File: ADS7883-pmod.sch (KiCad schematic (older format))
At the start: 16 parts, among them P1 CONN_01X03, P2 CONN_01X02, P3 CONN_01X02, P4 CONN_01X02, P5 CONN_02X06, U1 ref5050

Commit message: updated docs
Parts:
- U1: MOQ (none) -> Value; farnell # (none) -> 1439628; leadtime (none) -> Value; supplier (none) -> Value; supplier PN (none) -> Value
- adc1, adc2: MOQ (none) -> Value; farnell # (none) -> 2082426; leadtime (none) -> Value; supplier (none) -> Value; supplier PN (none) -> Value
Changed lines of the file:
@@
 F 2 "ADS7883:SOT-23-6" H 2950 2250 60  0001 C CNN
 F 3 "" H 2950 2250 60  0000 C CNN
+F 4 "2082426" H 2950 2250 60  0001 C CNN "farnell #"
+F 5 "Value" H 2950 2250 60  0001 C CNN "supplier"
+F 6 "Value" H 2950 2250 60  0001 C CNN "supplier PN"
+F 7 "Value" H 2950 2250 60  0001 C CNN "MOQ"
+F 8 "Value" H 2950 2250 60  0001 C CNN "leadtime"
 	1    2950 2250
 	1    0    0    -1
@@
 F 2 "ADS7883:SOT-23-6" H 2950 3550 60  0001 C CNN
 F 3 "" H 2950 3550 60  0000 C CNN
+F 4 "2082426" H 2950 3550 60  0001 C CNN "farnell #"
+F 5 "Value" H 2950 3550 60  0001 C CNN "supplier"
+F 6 "Value" H 2950 3550 60  0001 C CNN "supplier PN"
+F 7 "Value" H 2950 3550 60  0001 C CNN "MOQ"
+F 8 "Value" H 2950 3550 60  0001 C CNN "leadtime"
 	1    2950 3550
 	1    0    0    -1
@@
 F 2 "ADS7883:SOIC-8_3.9x4.9mm_Pitch1.27mm" H 9800 3850 60  0001 C CNN
 F 3 "" H 9800 3850 60  0000 C CNN
+F 4 "1439628" H 9800 3850 60  0001 C CNN "farnell #"
+F 5 "Value" H 9800 3850 60  0001 C CNN "supplier"
+F 6 "Value" H 9800 3850 60  0001 C CNN "supplier PN"
+F 7 "Value" H 9800 3850 60  0001 C CNN "MOQ"
+F 8 "Value" H 9800 3850 60  0001 C CNN "leadtime"
 	1    9800 3850
 	1    0    0    -1

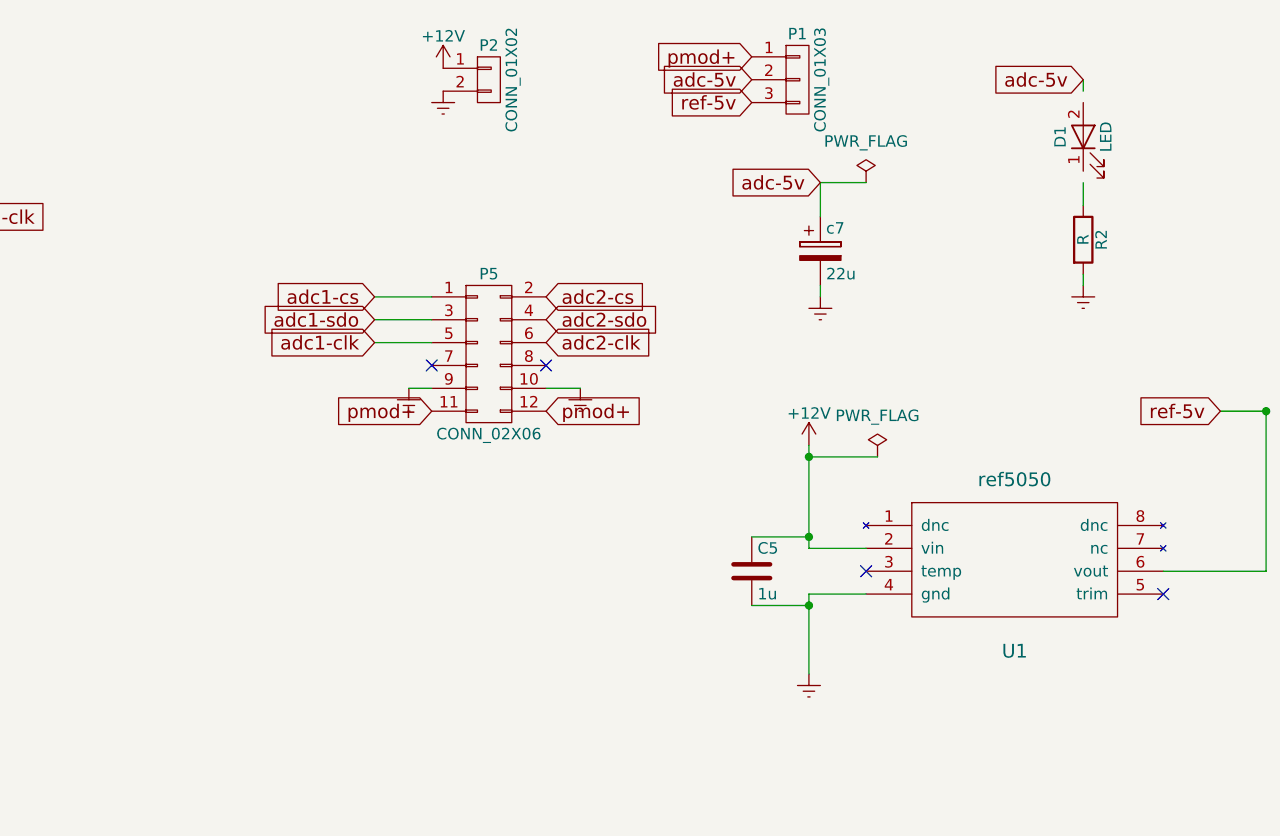
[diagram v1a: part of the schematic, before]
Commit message: convert to 4 layers and improve routing
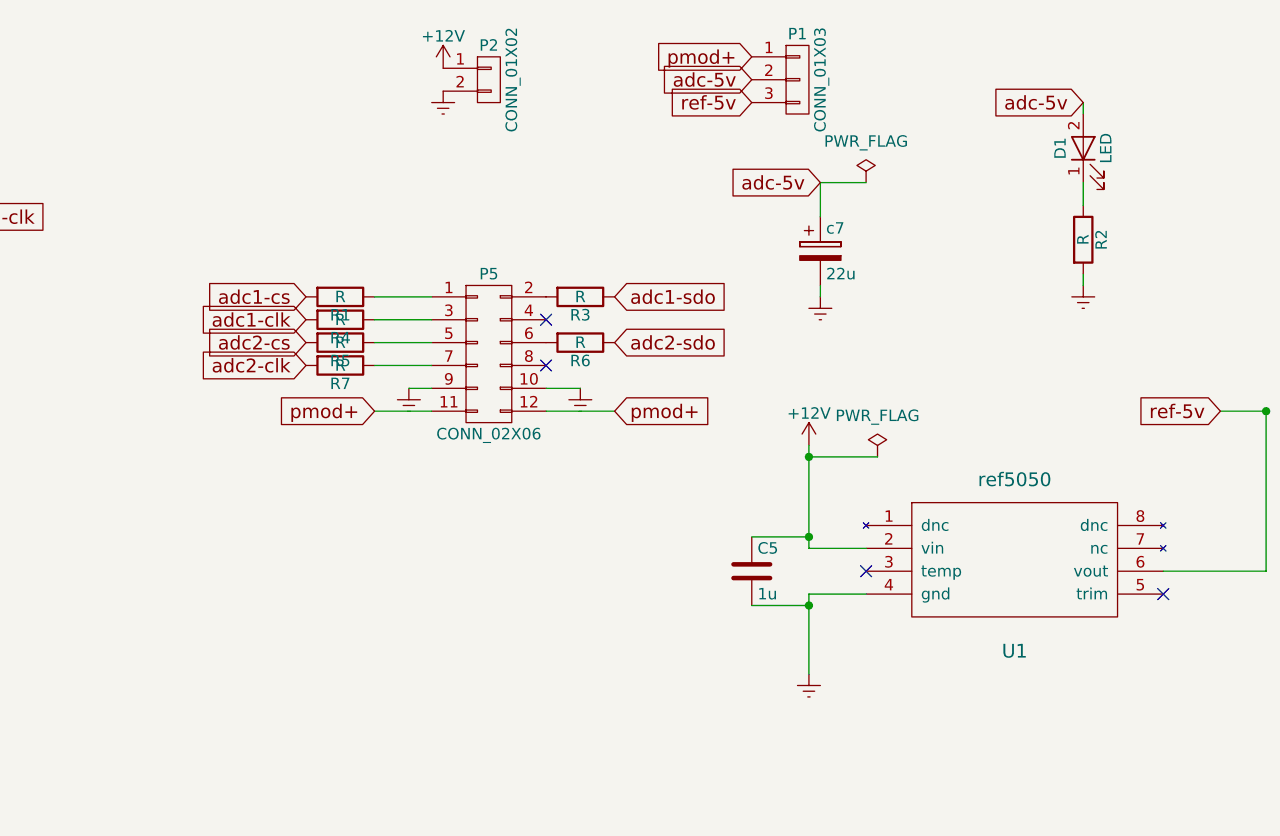
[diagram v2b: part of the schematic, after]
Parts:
- added R1, R3, R4, R5, R6, R7: R, Capacitors_SMD:C_0603_HandSoldering, symbol R
- C1, C2, C3, C4, C5: footprint ADS7883:C_1206_HandSoldering -> Capacitors_SMD:C_0603_HandSoldering
- D1: footprint ADS7883:LED-1206 -> LEDs:LED_0603_HandSoldering
- P3, P4: footprint ADS7883:Pin_Header_Straight_1x02 -> ADS7883:CON-SMA-EDGE
- R2: footprint ADS7883:R_1206_HandSoldering -> Capacitors_SMD:C_0603_HandSoldering
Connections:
- wire segments 45 -> 48
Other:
- moved on the sheet: D1
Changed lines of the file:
@@
 EESchema Schematic File Version 3
 LIBS:power
+LIBS:device
+LIBS:transistors
+LIBS:conn
+LIBS:linear
+LIBS:regul
 LIBS:74xx
+LIBS:cmos4000
+LIBS:adc-dac
+LIBS:memory
+LIBS:xilinx
+LIBS:microcontrollers
+LIBS:dsp
+LIBS:microchip
+LIBS:analog_switches
+LIBS:motorola
+LIBS:texas
+LIBS:intel
+LIBS:audio
+LIBS:interface
+LIBS:digital-audio
+LIBS:philips
+LIBS:display
+LIBS:cypress
+LIBS:siliconi
+LIBS:opto
+LIBS:atmel
+LIBS:contrib
+LIBS:valves
 LIBS:ads7883
 LIBS:ref5050
@@
 encoding utf-8
 Sheet 1 1
-Title ""
-Date ""
-Rev ""
-Comp ""
+Title "2xADS7883"
+Date "2019-04-25"
+Rev "v2"
+Comp "Pancom"
 Comment1 ""
 Comment2 ""
@@
 	1    0    0    -1
 $EndComp
-Text GLabel 6950 2650 0    60   Input ~ 0
+Text GLabel 8000 2550 2    60   Input ~ 0
 adc1-sdo
-Text GLabel 7700 2650 2    60   Input ~ 0
+Text GLabel 8000 2750 2    60   Input ~ 0
 adc2-sdo
 Text GLabel 3850 2000 2    60   Input ~ 0
@@
 F 0 "P3" H 1700 2650 50  0000 C CNN
 F 1 "CONN_01X02" V 1800 2500 50  0000 C CNN
-F 2 "ADS7883:Pin_Header_Straight_1x02" H 1700 2500 60  0001 C CNN
+F 2 "ADS7883:CON-SMA-EDGE" H 1700 2500 60  0001 C CNN
 F 3 "" H 1700 2500 60  0000 C CNN
 F 4 "Value" H 1700 2500 60  0001 C CNN "supplier"
@@
 F 0 "P4" H 1750 4000 50  0000 C CNN
 F 1 "CONN_01X02" V 1850 3850 50  0000 C CNN
-F 2 "ADS7883:Pin_Header_Straight_1x02" H 1750 3850 60  0001 C CNN
+F 2 "ADS7883:CON-SMA-EDGE" H 1750 3850 60  0001 C CNN
 F 3 "" H 1750 3850 60  0000 C CNN
 F 4 "Value" H 1750 3850 60  0001 C CNN "supplier"
@@
 F 0 "C1" H 1775 1700 50  0000 L CNN
 F 1 "1u" H 1775 1500 50  0000 L CNN
-F 2 "ADS7883:C_1206_HandSoldering" H 1788 1450 30  0001 C CNN
+F 2 "Capacitors_SMD:C_0603_HandSoldering" H 1788 1450 30  0001 C CNN
 F 3 "" H 1750 1600 60  0000 C CNN
 	1    1750 1600
@@
 F 0 "C3" H 2075 1700 50  0000 L CNN
 F 1 "10n" H 2075 1500 50  0000 L CNN
-F 2 "ADS7883:C_1206_HandSoldering" H 2088 1450 30  0001 C CNN
+F 2 "Capacitors_SMD:C_0603_HandSoldering" H 2088 1450 30  0001 C CNN
 F 3 "" H 2050 1600 60  0000 C CNN
 	1    2050 1600
@@
 F 0 "C2" H 1825 3050 50  0000 L CNN
 F 1 "1u" H 1825 2850 50  0000 L CNN
-F 2 "ADS7883:C_1206_HandSoldering" H 1838 2800 30  0001 C CNN
+F 2 "Capacitors_SMD:C_0603_HandSoldering" H 1838 2800 30  0001 C CNN
 F 3 "" H 1800 2950 60  0000 C CNN
 	1    1800 2950
@@
 F 0 "C4" H 2125 3050 50  0000 L CNN
 F 1 "10n" H 2125 2850 50  0000 L CNN
-F 2 "ADS7883:C_1206_HandSoldering" H 2138 2800 30  0001 C CNN
+F 2 "Capacitors_SMD:C_0603_HandSoldering" H 2138 2800 30  0001 C CNN
 F 3 "" H 2100 2950 60  0000 C CNN
 	1    2100 2950
@@
 L LED D1
 U 1 1 57CF06F4
-P 10050 1850
-F 0 "D1" H 10050 1950 50  0000 C CNN
-F 1 "LED" H 10050 1750 50  0000 C CNN
-F 2 "ADS7883:LED-1206" H 10050 1850 60  0001 C CNN
-F 3 "" H 10050 1850 60  0000 C CNN
-	1    10050 1850
+P 10050 1900
+F 0 "D1" H 10050 2000 50  0000 C CNN
+F 1 "LED" H 10050 1800 50  0000 C CNN
+F 2 "LEDs:LED_0603_HandSoldering" H 10050 1900 60  0001 C CNN
+F 3 "" H 10050 1900 60  0000 C CNN
+	1    10050 1900
 	0    -1   -1   0
 $EndComp
@@
 F 0 "R2" V 10130 2300 50  0000 C CNN
 F 1 "R" V 10050 2300 50  0000 C CNN
-F 2 "ADS7883:R_1206_HandSoldering" V 9980 2300 30  0001 C CNN
+F 2 "Capacitors_SMD:C_0603_HandSoldering" V 9980 2300 30  0001 C CNN
 F 3 "" H 10050 2300 30  0000 C CNN
 	1    10050 2300
@@
 	8900 2050 8900 2200
 Wire Wire Line
-	10050 1650 10050 1600
+	10050 1750 10050 1700
 Wire Wire Line
 	10050 2150 10050 2050
@@
 $EndComp
 Wire Wire Line
-	8850 4200 8850 3850
+	8850 3850 8850 4200
 Wire Wire Line
 	8850 3850 9100 3850
@@
 F 0 "C5" H 8625 3850 50  0000 L CNN
 F 1 "1u" H 8625 3650 50  0000 L CNN
-F 2 "ADS7883:C_1206_HandSoldering" H 8638 3600 30  0001 C CNN
+F 2 "Capacitors_SMD:C_0603_HandSoldering" H 8638 3600 30  0001 C CNN
 F 3 "" H 8600 3750 60  0000 C CNN
 	1    8600 3750
@@
 	1    0    0    -1
 $EndComp
-Text GLabel 10050 1600 0    60   Input ~ 0
+Text GLabel 10050 1700 0    60   Input ~ 0
 adc-5v
 $Comp
@@
 Text GLabel 4650 3500 2    60   Input ~ 0
 adc2-clk
-Text GLabel 6950 2550 0    60   Input ~ 0
+Text GLabel 6650 2550 0    60   Input ~ 0
 adc1-cs
-Text GLabel 6950 2750 0    60   Input ~ 0
+Text GLabel 6650 2650 0    60   Input ~ 0
 adc1-clk
-Text GLabel 7700 2750 2    60   Input ~ 0
+Text GLabel 6650 2850 0    60   Input ~ 0
 adc2-clk
-Text GLabel 7700 2550 2    60   Input ~ 0
+Text GLabel 6650 2750 0    60   Input ~ 0
 adc2-cs
-Text GLabel 7200 3050 0    60   Input ~ 0
+Text GLabel 6950 3050 0    60   Input ~ 0
 pmod+
-Text GLabel 7700 3050 2    60   Input ~ 0
+Text GLabel 8000 3050 2    60   Input ~ 0
 pmod+
+NoConn ~ 7700 2650
 NoConn ~ 7700 2850
-NoConn ~ 7200 2850
 NoConn ~ 4900 2250
+Wire Wire Line
+	6950 3050 7200 3050
+Wire Wire Line
+	7700 3050 8000 3050
+$Comp
+L R R1
+U 1 1 5CC1E070
+P 6800 2550
+F 0 "R1" V 6880 2550 50  0000 C CNN
+F 1 "R" V 6800 2550 50  0000 C CNN
+F 2 "Capacitors_SMD:C_0603_HandSoldering" V 6730 2550 30  0001 C CNN
+F 3 "" H 6800 2550 30  0000 C CNN
+	1    6800 2550
+	0    1    1    0
+$EndComp
+$Comp
+L R R4
+U 1 1 5CC1E0FF
+P 6800 2650
+F 0 "R4" V 6880 2650 50  0000 C CNN
+F 1 "R" V 6800 2650 50  0000 C CNN
+F 2 "Capacitors_SMD:C_0603_HandSoldering" V 6730 2650 30  0001 C CNN
+F 3 "" H 6800 2650 30  0000 C CNN
+	1    6800 2650
+	0    1    1    0
+$EndComp
+$Comp
+L R R5
+U 1 1 5CC1E137
+P 6800 2750
+F 0 "R5" V 6880 2750 50  0000 C CNN
+F 1 "R" V 6800 2750 50  0000 C CNN
+F 2 "Capacitors_SMD:C_0603_HandSoldering" V 6730 2750 30  0001 C CNN
+F 3 "" H 6800 2750 30  0000 C CNN
+	1    6800 2750
+	0    1    1    0
+$EndComp
+$Comp
+L R R6
+U 1 1 5CC1E171
+P 7850 2750
+F 0 "R6" V 7930 2750 50  0000 C CNN
+F 1 "R" V 7850 2750 50  0000 C CNN
+F 2 "Capacitors_SMD:C_0603_HandSoldering" V 7780 2750 30  0001 C CNN
+F 3 "" H 7850 2750 30  0000 C CNN
+	1    7850 2750
+	0    1    1    0
+$EndComp
+$Comp
+L R R3
+U 1 1 5CC1E1C9
+P 7850 2550
+F 0 "R3" V 7930 2550 50  0000 C CNN
+F 1 "R" V 7850 2550 50  0000 C CNN
+F 2 "Capacitors_SMD:C_0603_HandSoldering" V 7780 2550 30  0001 C CNN
+F 3 "" H 7850 2550 30  0000 C CNN
+	1    7850 2550
+	0    1    1    0
+$EndComp
+$Comp
+L R R7
+U 1 1 5CC1E231
+P 6800 2850
+F 0 "R7" V 6880 2850 50  0000 C CNN
+F 1 "R" V 6800 2850 50  0000 C CNN
+F 2 "Capacitors_SMD:C_0603_HandSoldering" V 6730 2850 30  0001 C CNN
+F 3 "" H 6800 2850 30  0000 C CNN
+	1    6800 2850
+	0    1    1    0
+$EndComp
+Wire Wire Line
+	6950 2850 7200 2850
 $EndSCHEMATC

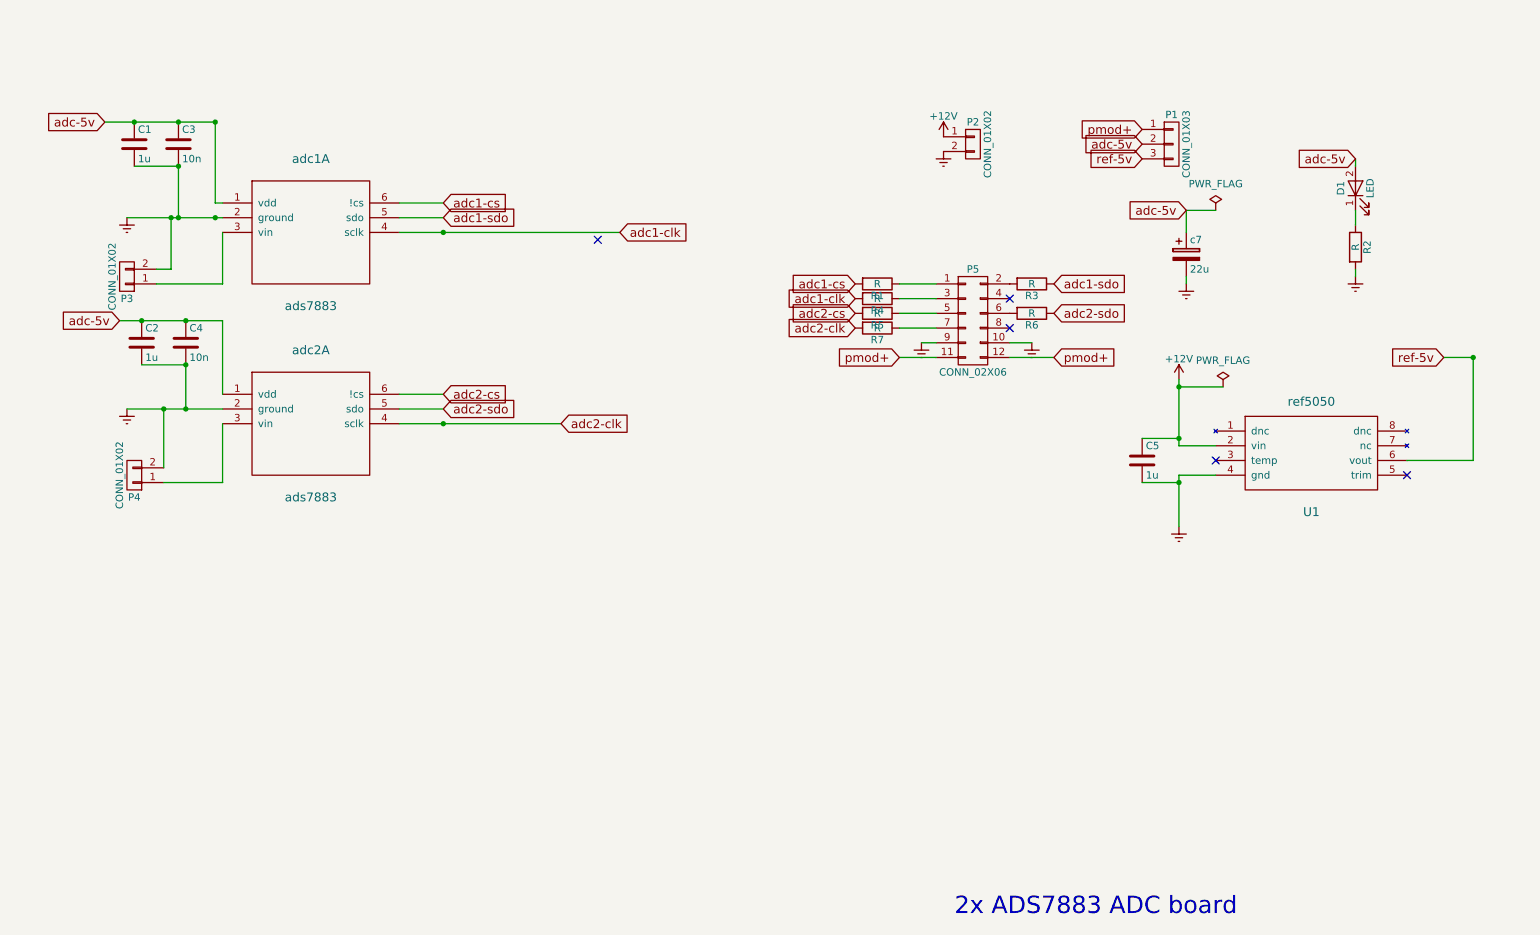
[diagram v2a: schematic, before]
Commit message: got rid of 1 ADC and added phantom and shield can
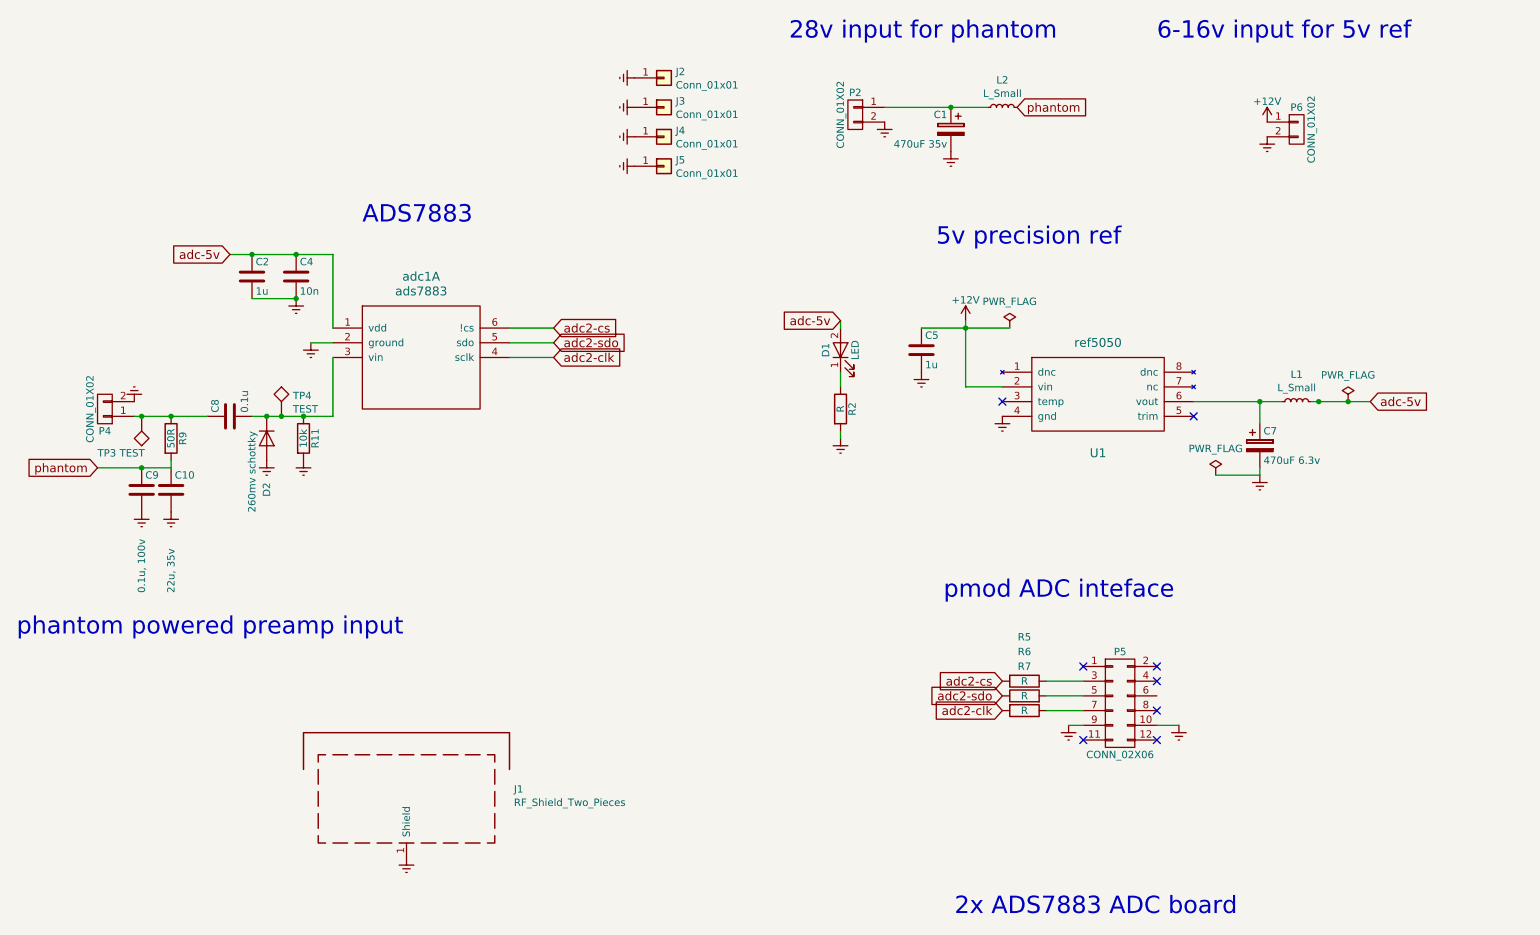
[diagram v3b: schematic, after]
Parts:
- removed C1: 1u, Capacitors_SMD:C_0603_HandSoldering, symbol C
- removed C3: 10n, Capacitors_SMD:C_0603_HandSoldering, symbol C
- removed P1: CONN_01X03, ADS7883:Pin_Header_Straight_1x03, symbol CONN_01X03
- removed P3: CONN_01X02, ADS7883:CON-SMA-EDGE, symbol CONN_01X02
- removed R1, R3, R4: R, Capacitors_SMD:C_0603_HandSoldering, symbol R
- removed adc1: ads7883, ADS7883:SOT-23-6, symbol ads7883
- added C1: 470uF 35v, Capacitors_SMD:CP_Elec_10x10, symbol CP
- added C10: 22u, 35v, Capacitors_Tantalum_SMD:CP_Tantalum_Case-D_EIA-7343-31_Hand, symbol C
- added C8: 0.1u, Capacitors_SMD:C_0603_HandSoldering, symbol C
- added C9: 0.1u, 100v, Capacitors_SMD:C_0603_HandSoldering, symbol C
- added D2: 260mv schottky, Diodes_SMD:D_SOT-23_ANK, symbol D
- added J1: RF_Shield_Two_Pieces, Shielding_Cabinets:Laird_Technologies_BMI-S-102_16.50x16.50mm, symbol RF_Shield_Two_Pieces
- added J2, J3, J4, J5: Conn_01x01, Mounting_Holes:MountingHole_3.2mm_M3_DIN965_Pad, symbol Conn_01x01
- added L1, L2: L_Small, Inductors_SMD:L_0603_HandSoldering, symbol L_Small
- added P6: CONN_01X02, ADS7883:Pin_Header_Straight_1x02, symbol CONN_01X02
- added R11: 10k, Capacitors_SMD:C_0603_HandSoldering, symbol R
- added R9: 50R, Resistors_SMD:R_1206_HandSoldering, symbol R
- added TP3, TP4: TEST, Connectors_TestPoints:Test_Point_Pad_1.0x1.0mm, symbol TEST
- C7: renamed from c7; value 22u -> 470uF 6.3v; footprint ADS7883:c_elec_6.3x7.7 -> Capacitors_SMD:CP_Elec_6.3x7.7; MOQ (none) -> Value; farnell # (none) -> 2065955; leadtime (none) -> Value; supplier (none) -> Value; supplier PN (none) -> Value
- renumbered adc2 to adc1
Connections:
- net +12V: now also P6.1 (P1); no longer P2.1 (P1)
- net Earth: now also C1.2, C10.2, C9.2, D2.2 (A), J1.1 (Shield), J2.1 (Pin_1), J3.1 (Pin_1), J4.1 (Pin_1), J5.1 (Pin_1), P6.2 (P2), R11.2
- net adc-5v: now also L1.2; no longer C7.1
- net at P5.3 (P3): now also R5.1
- net at P5.5 (P5): now also R6.2; no longer R5.1
- net at P5.6 (P6): no longer R6.2
- net at adc1.3 (vin): now also C8.2, D2.1 (K), R11.1, TP4.1; no longer P4.1 (P1)
- net pmod+: no longer names the net of P5.11 (P11)
- net pmod+: no longer P5.12 (P12)
- net ref-5v: no longer names the net of U1.6 (vout)
- net ref-5v: now also C7.1, L1.1
- new net: C8.1, P4.1 (P1), R9.1, TP3.1
- new net: C1.1, L2.2, P2.1 (P1)
- new net phantom: C10.1, C9.1, L2.1, R9.2
- no-connect marks 5 -> 8
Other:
- note added: "28v input for phantom"
- note added: "5v precision ref"
- note added: "6-16v input for 5v ref"
- note added: "ADS7883\n"
- note added: "phantom powered preamp input\n"
- note added: "pmod ADC inteface"
- moved on the sheet: C2, C4, C5, C7, D1, P2, P4, P5, R2, R5, R6, R7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
